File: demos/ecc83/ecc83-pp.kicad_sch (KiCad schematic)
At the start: 15 parts, among them P1 IN, P2 OUT, P3 POWER, P4 CONN_2, P5 MOUNTING_HOLE, P6 MOUNTING_HOLE, P7 MOUNTING_HOLE, P8 MOUNTING_HOLE, U1 ECC83

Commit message: Demos update
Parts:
- U: renamed from R1; value 1.5K -> (none); footprint Resistor_THT:R_Axial_DIN0207_L6.3mm_D2.5mm_P7.62mm_Horizontal -> (none)
- U: renamed from R2; value 1.5K -> (none); footprint Resistor_THT:R_Axial_DIN0207_L6.3mm_D2.5mm_P7.62mm_Horizontal -> (none)
- U: renamed from R4; value 47K -> (none); footprint Resistor_THT:R_Axial_DIN0207_L6.3mm_D2.5mm_P7.62mm_Horizontal -> (none)
- U: renamed from R3; value 100K -> (none); footprint Resistor_THT:R_Axial_DIN0207_L6.3mm_D2.5mm_P7.62mm_Horizontal -> (none)
- U: renamed from C2; value 680nF -> (none); footprint Capacitor_THT:C_Disc_D4.7mm_W2.5mm_P5.00mm -> (none)
- U: renamed from P1; value IN -> (none); footprint TerminalBlock_Altech:Altech_AK300_1x02_P5.00mm_45-Degree -> (none)
- U: renamed from P2; value OUT -> (none); footprint TerminalBlock_Altech:Altech_AK300_1x02_P5.00mm_45-Degree -> (none)
- U: renamed from P3; value POWER -> (none); footprint TerminalBlock_Altech:Altech_AK300_1x02_P5.00mm_45-Degree -> (none)
- U: renamed from C1; value 10uF -> (none); footprint Capacitor_THT:CP_Radial_D10.0mm_P5.00mm -> (none)
- U: renamed from P4; value CONN_2 -> (none); footprint TerminalBlock_Altech:Altech_AK300_1x02_P5.00mm_45-Degree -> (none)
- U: renamed from U1; value ECC83 -> (none); footprint Valve:Valve_ECC-83-1 -> (none)
- U: renamed from P5; value MOUNTING_HOLE -> (none); footprint MountingHole:MountingHole_3.2mm_M3_DIN965_Pad -> (none)
- U: renamed from P6; value MOUNTING_HOLE -> (none); footprint MountingHole:MountingHole_3.2mm_M3_DIN965_Pad -> (none)
- U: renamed from P7; value MOUNTING_HOLE -> (none); footprint MountingHole:MountingHole_3.2mm_M3_DIN965_Pad -> (none)
- U: renamed from P8; value MOUNTING_HOLE -> (none); footprint MountingHole:MountingHole_3.2mm_M3_DIN965_Pad -> (none)
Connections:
- net at U.1, U.7 (G): now also U.6 (A); no longer U.1 (A)
- net at U.1: now also U.8 (K); no longer U.3 (K)
- net at U.1, U.2 (PM): now also U.7 (G); no longer U.2 (G)
- net at U.1 (P1): no longer U.9 (F2)
- now unconnected: U.2 (PM)

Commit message: Demos update.
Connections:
- net at U.1, U.7 (G): now also U.1 (A); no longer U.6 (A)
- net at U.1: now also U.3 (K); no longer U.8 (K)
- net at U.1, U.2 (PM): now also U.2 (G); no longer U.7 (G)
- net at U.1 (P1): now also U.9 (F2)
- net at U.2 (PM): now also U.4 (F1), U.5 (F1)
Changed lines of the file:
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@@
-(kicad_sch (version 20220404) (generator eeschema)
+(kicad_sch (version 20220822) (generator eeschema)
   (paper "A4")
   (title_block
@@
     (pin "7")
     (pin "8")
+  )
+  (symbol (lib_id "ecc83_schlib:ECC83") (at 157.48 107.95 0) (unit 2)
+    (in_bom yes) (on_board yes)
+    (default_instance (reference "U") (unit 1) (value "") (footprint ""))
+    (property "Reference" "U" (id 0) (at 161.29 99.06 0)
+      (effects (font (size 1.27 1.27)))
+    )
+    (property "Value" "" (id 1) (at 162.56 116.84 0)
+      (effects (font (size 1.27 1.27)))
+    )
+    (property "Footprint" "" (id 2) (at 162.56 118.11 0)
+      (effects (font (size 0.762 0.762)) hide)
+    )
+    (property "Datasheet" "" (id 3) (at 157.48 107.95 0)
+      (effects (font (size 1.524 1.524)) hide)
+    )
     (pin "1")
     (pin "2")
     (pin "3")
+  )
+  (symbol (lib_id "ecc83_schlib:ECC83") (at 63.5 74.93 0) (unit 3)
+    (in_bom yes) (on_board yes)
+    (default_instance (reference "U") (unit 1) (value "") (footprint ""))
+    (property "Reference" "U" (id 0) (at 63.5 63.5 0)
+      (effects (font (size 1.27 1.27)))
+    )
+    (property "Value" "" (id 1) (at 63.5 66.04 0)
+      (effects (font (size 1.27 1.27)))
+    )
+    (property "Footprint" "" (id 2) (at 57.15 74.93 90)
+      (effects (font (size 0.762 0.762)) hide)
+    )
+    (property "Datasheet" "" (id 3) (at 63.5 74.93 0)
+      (effects (font (size 1.524 1.524)) hide)
+    )
     (pin "4")
     (pin "5")
-    (pin "9")
-  )
-  (symbol (lib_id "ecc83_schlib:ECC83") (at 157.48 107.95 0) (unit 1)
-    (in_bom yes) (on_board yes)
-    (default_instance (reference "U") (unit 1) (value "") (footprint ""))
-    (property "Reference" "U" (id 0) (at 161.29 99.06 0)
-      (effects (font (size 1.27 1.27)))
-    )
-    (property "Value" "" (id 1) (at 162.56 116.84 0)
-      (effects (font (size 1.27 1.27)))
-    )
-    (property "Footprint" "" (id 2) (at 162.56 118.11 0)
-      (effects (font (size 0.762 0.762)) hide)
-    )
-    (property "Datasheet" "" (id 3) (at 157.48 107.95 0)
-      (effects (font (size 1.524 1.524)) hide)
-    )
-    (pin "6")
-    (pin "7")
-    (pin "8")
-    (pin "1")
-    (pin "2")
-    (pin "3")
-    (pin "4")
-    (pin "5")
-    (pin "9")
-  )
-  (symbol (lib_id "ecc83_schlib:ECC83") (at 63.5 74.93 0) (unit 1)
-    (in_bom yes) (on_board yes)
-    (default_instance (reference "U") (unit 1) (value "") (footprint ""))
-    (property "Reference" "U" (id 0) (at 63.5 63.5 0)
-      (effects (font (size 1.27 1.27)))
-    )
-    (property "Value" "" (id 1) (at 63.5 66.04 0)
-      (effects (font (size 1.27 1.27)))
-    )
-    (property "Footprint" "" (id 2) (at 57.15 74.93 90)
-      (effects (font (size 0.762 0.762)) hide)
-    )
-    (property "Datasheet" "" (id 3) (at 63.5 74.93 0)
-      (effects (font (size 1.524 1.524)) hide)
-    )
-    (pin "6")
-    (pin "7")
-    (pin "8")
-    (pin "1")
-    (pin "2")
-    (pin "3")
-    (pin "4")
-    (pin "5")

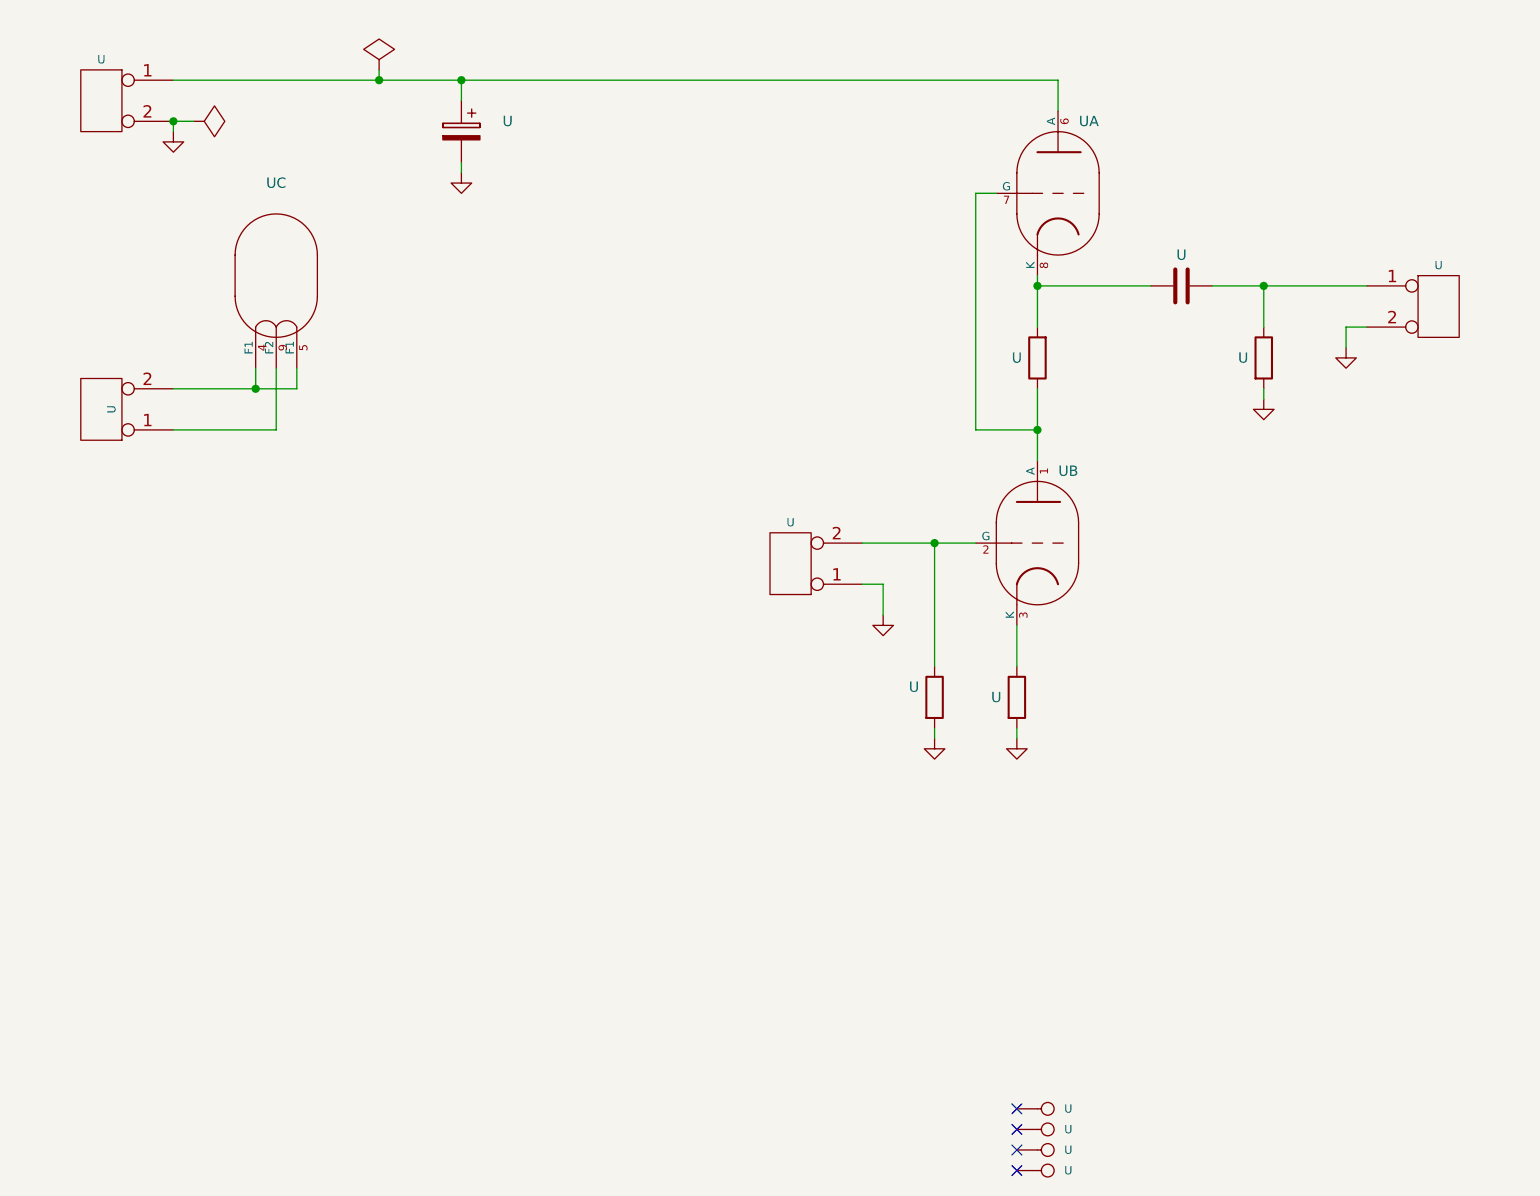
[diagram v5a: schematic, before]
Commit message: Update demos using latest file formats.
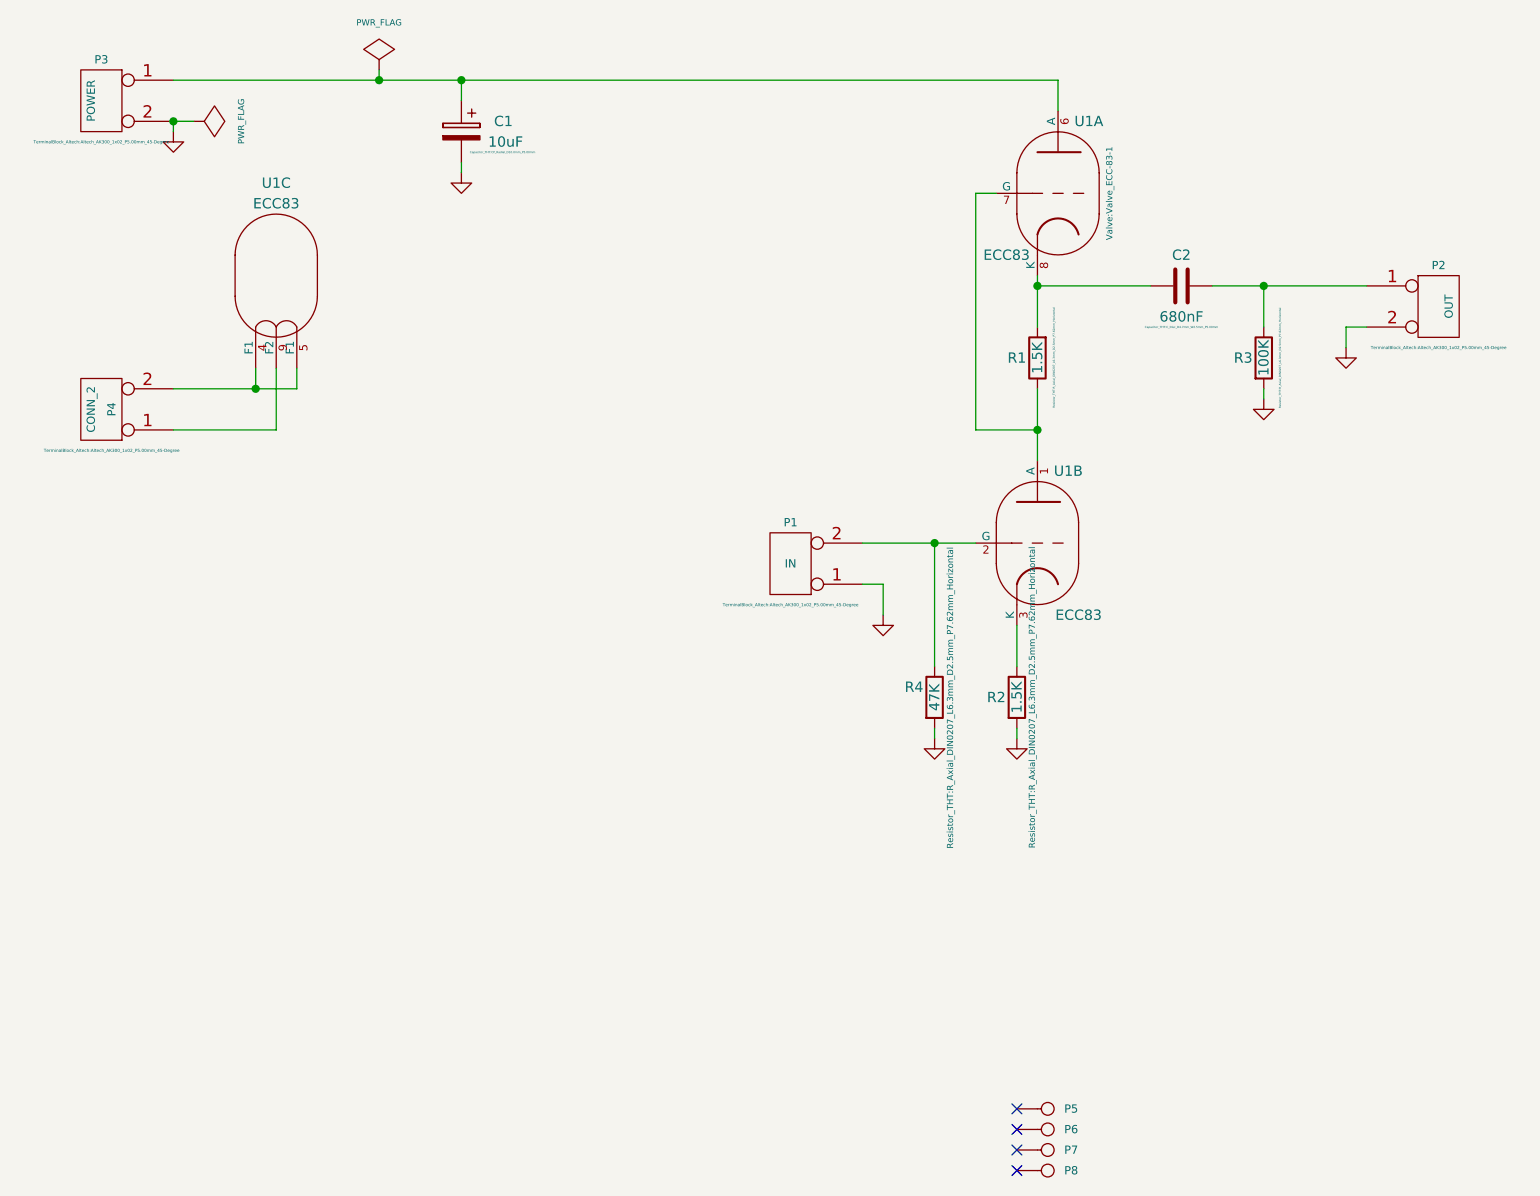
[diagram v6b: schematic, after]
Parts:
- C1: renamed from U; value (none) -> 10uF; footprint (none) -> Capacitor_THT:CP_Radial_D10.0mm_P5.00mm
- C2: renamed from U; value (none) -> 680nF; footprint (none) -> Capacitor_THT:C_Disc_D4.7mm_W2.5mm_P5.00mm
- P1: renamed from U; value (none) -> IN; footprint (none) -> TerminalBlock_Altech:Altech_AK300_1x02_P5.00mm_45-Degree
- P2: renamed from U; value (none) -> OUT; footprint (none) -> TerminalBlock_Altech:Altech_AK300_1x02_P5.00mm_45-Degree
- P3: renamed from U; value (none) -> POWER; footprint (none) -> TerminalBlock_Altech:Altech_AK300_1x02_P5.00mm_45-Degree
- P4: renamed from U; value (none) -> CONN_2; footprint (none) -> TerminalBlock_Altech:Altech_AK300_1x02_P5.00mm_45-Degree
- P5, P6, P7, P8: renamed from U; value (none) -> MOUNTING_HOLE; footprint (none) -> MountingHole:MountingHole_3.2mm_M3_DIN965_Pad
- R1, R2: renamed from U; value (none) -> 1.5K; footprint (none) -> Resistor_THT:R_Axial_DIN0207_L6.3mm_D2.5mm_P7.62mm_Horizontal
- R3: renamed from U; value (none) -> 100K; footprint (none) -> Resistor_THT:R_Axial_DIN0207_L6.3mm_D2.5mm_P7.62mm_Horizontal
- R4: renamed from U; value (none) -> 47K; footprint (none) -> Resistor_THT:R_Axial_DIN0207_L6.3mm_D2.5mm_P7.62mm_Horizontal
- U1: renamed from U; value (none) -> ECC83; footprint (none) -> Valve:Valve_ECC-83-1
